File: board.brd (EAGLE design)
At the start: 50 x 50 mm, 28 parts

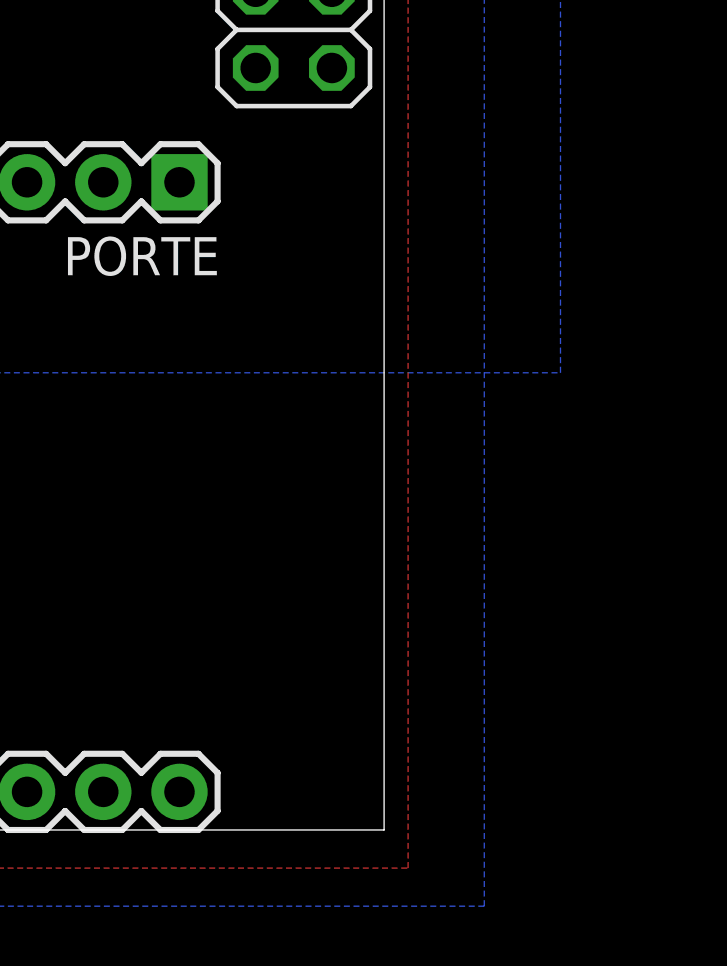
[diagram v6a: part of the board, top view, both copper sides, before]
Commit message: connecting rest of the ports
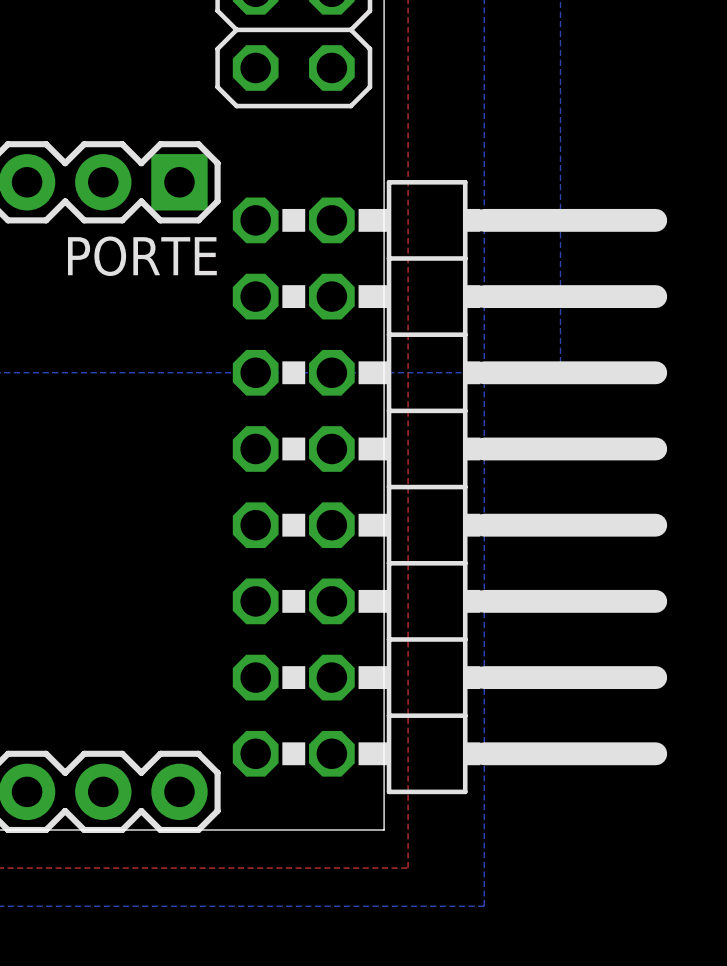
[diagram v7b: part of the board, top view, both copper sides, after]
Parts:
- added JP2: (no value), pinhead:2X08/90
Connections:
- removed net SCL: PORTE.2
- removed net SDA: PORTE.1
- new net PB1/VBAT_SENSE: JP2.3, PORTB.2
- new net PB2: JP2.5, PORTB.3
- new net PB3: JP2.7, PORTB.4
- new net PD0: JP2.9, PORTD.1
- new net PD1: JP2.11, PORTD.2
- new net PD5: JP2.15, PORTD.6
- new net PE1/SCL: JP2.4, PORTE.2
- new net PE1/SDA: JP2.2, PORTE.1
- new net PE2: JP2.6, PORTE.3
- new net PE3: JP2.8, PORTE.4
- net +3V3: now also JP2.12
- net GND: now also JP2.10, JP2.13
- net PB0/XMEGA_AREF: now also JP2.1
- net VBAT_SENSE: no longer PORTB.2
- net XMEGA_RX1: now also JP2.14
- net XMEGA_TX1: now also JP2.16
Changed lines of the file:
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@@
 <attribute name="VALUE" x="22.225" y="45.339" size="1.27" layer="27" rot="R270"/>
+</element>
+<element name="JP2" library="pinhead" package="2X08/90" value="" x="52.07" y="11.43" smashed="yes" rot="R270">
+<attribute name="VALUE" x="48.26" y="-0.635" size="1.27" layer="27"/>
 </element>
 </elements>
@@
 <contactref element="PGND_GND" pad="1"/>
 <contactref element="AGND_GND" pad="2"/>
+<contactref element="JP2" pad="10"/>
+<contactref element="JP2" pad="13"/>
 </signal>
 <signal name="PDI_DATA">
@@
 <wire x1="5.59" y1="26.465" x2="33.02" y2="1.27" width="0" layer="19" extent="1-1"/>
 </signal>
-<signal name="SDA">
+<signal name="PE1/SDA">
 <contactref element="PORTE" pad="1"/>
-</signal>
-<signal name="SCL">
+<contactref element="JP2" pad="2"/>
+<wire x1="43.18" y1="21.59" x2="48.26" y2="20.32" width="0" layer="19" extent="1-1"/>
+</signal>
+<signal name="PE1/SCL">
 <contactref element="PORTE" pad="2"/>
+<contactref element="JP2" pad="4"/>
+<wire x1="40.64" y1="21.59" x2="48.26" y2="17.78" width="0" layer="19" extent="1-1"/>
 </signal>
 <signal name="VXMEGA_USB">
@@
 <signal name="XMEGA_TX1">
 <contactref element="PORTC" pad="8"/>
+<contactref element="JP2" pad="16"/>
+<wire x1="22.86" y1="1.27" x2="48.26" y2="2.54" width="0" layer="19" extent="1-1"/>
 </signal>
 <signal name="XMEGA_RX1">
 <contactref element="PORTC" pad="7"/>
+<contactref element="JP2" pad="14"/>
+<wire x1="20.32" y1="1.27" x2="48.26" y2="5.08" width="0" layer="19" extent="1-1"/>
 </signal>
 <signal name="PGND" class="1">
@@
 <contactref element="R2" pad="2"/>
 <contactref element="C1" pad="1"/>
-<contactref element="PORTB" pad="2"/>
-<wire x1="10.16" y1="21.59" x2="9.765" y2="24.13" width="0" layer="19" extent="16-16"/>
-<wire x1="10.16" y1="18.73" x2="10.16" y2="21.59" width="0" layer="19" extent="16-16"/>
+<wire x1="10.16" y1="18.73" x2="9.765" y2="24.13" width="0" layer="19" extent="16-16"/>
 <wire x1="7.62" y1="18.73" x2="10.16" y2="18.73" width="0" layer="19" extent="16-16"/>
 </signal>
@@
 <contactref element="SJ2" pad="3"/>
 <contactref element="XBEE" pad="1"/>
+<contactref element="JP2" pad="12"/>
 <wire x1="1.59" y1="26.465" x2="22.86" y2="44.196" width="0" layer="19" extent="1-1"/>
+<wire x1="48.26" y1="7.62" x2="22.86" y2="44.196" width="0" layer="19" extent="1-1"/>
 </signal>
 <signal name="LED0R" class="1">
@@
 <contactref element="PORTB" pad="1"/>
 <contactref element="XBEE" pad="14"/>
-<wire x1="12.7" y1="21.59" x2="13.59" y2="48.465" width="0" layer="19" extent="1-1"/>
+<contactref element="JP2" pad="1"/>
+<wire x1="12.7" y1="21.59" x2="45.72" y2="20.32" width="0" layer="19" extent="1-1"/>
+<wire x1="13.59" y1="48.465" x2="12.7" y2="21.59" width="0" layer="19" extent="1-1"/>
 </signal>
 <signal name="XBEE_RESET">
@@
 <wire x1="9.59" y1="26.465" x2="35.56" y2="1.27" width="0" layer="19" extent="1-1"/>
 </signal>
+<signal name="PB1/VBAT_SENSE">
+<contactref element="PORTB" pad="2"/>
+<contactref element="JP2" pad="3"/>
+<wire x1="10.16" y1="21.59" x2="45.72" y2="17.78" width="0" layer="19" extent="1-1"/>
+</signal>
+<signal name="PB2">
+<contactref element="PORTB" pad="3"/>
+<contactref element="JP2" pad="5"/>
+<wire x1="7.62" y1="21.59" x2="45.72" y2="15.24" width="0" layer="19" extent="1-1"/>
+</signal>
+<signal name="PB3">
+<contactref element="PORTB" pad="4"/>
+<contactref element="JP2" pad="7"/>
+<wire x1="5.08" y1="21.59" x2="45.72" y2="12.7" width="0" layer="19" extent="1-1"/>
+</signal>
+<signal name="PE2">
+<contactref element="PORTE" pad="3"/>
+<contactref element="JP2" pad="6"/>
+<wire x1="38.1" y1="21.59" x2="48.26" y2="15.24" width="0" layer="19" extent="1-1"/>
+</signal>
+<signal name="PE3">
+<contactref element="PORTE" pad="4"/>
+<contactref element="JP2" pad="8"/>
+<wire x1="35.56" y1="21.59" x2="48.26" y2="12.7" width="0" layer="19" extent="1-1"/>
+</signal>
+<signal name="PD0">
+<contactref element="PORTD" pad="1"/>
+<contactref element="JP2" pad="9"/>
+<wire x1="25.4" y1="1.27" x2="45.72" y2="10.16" width="0" layer="19" extent="1-1"/>
+</signal>
+<signal name="PD1">
+<contactref element="PORTD" pad="2"/>
+<contactref element="JP2" pad="11"/>
+<wire x1="27.94" y1="1.27" x2="45.72" y2="7.62" width="0" layer="19" extent="1-1"/>
+</signal>
+<signal name="PD5">
+<contactref element="PORTD" pad="6"/>
+<contactref element="JP2" pad="15"/>
+<wire x1="38.1" y1="1.27" x2="45.72" y2="2.54" width="0" layer="19" extent="1-1"/>
+</signal>
 </signals>

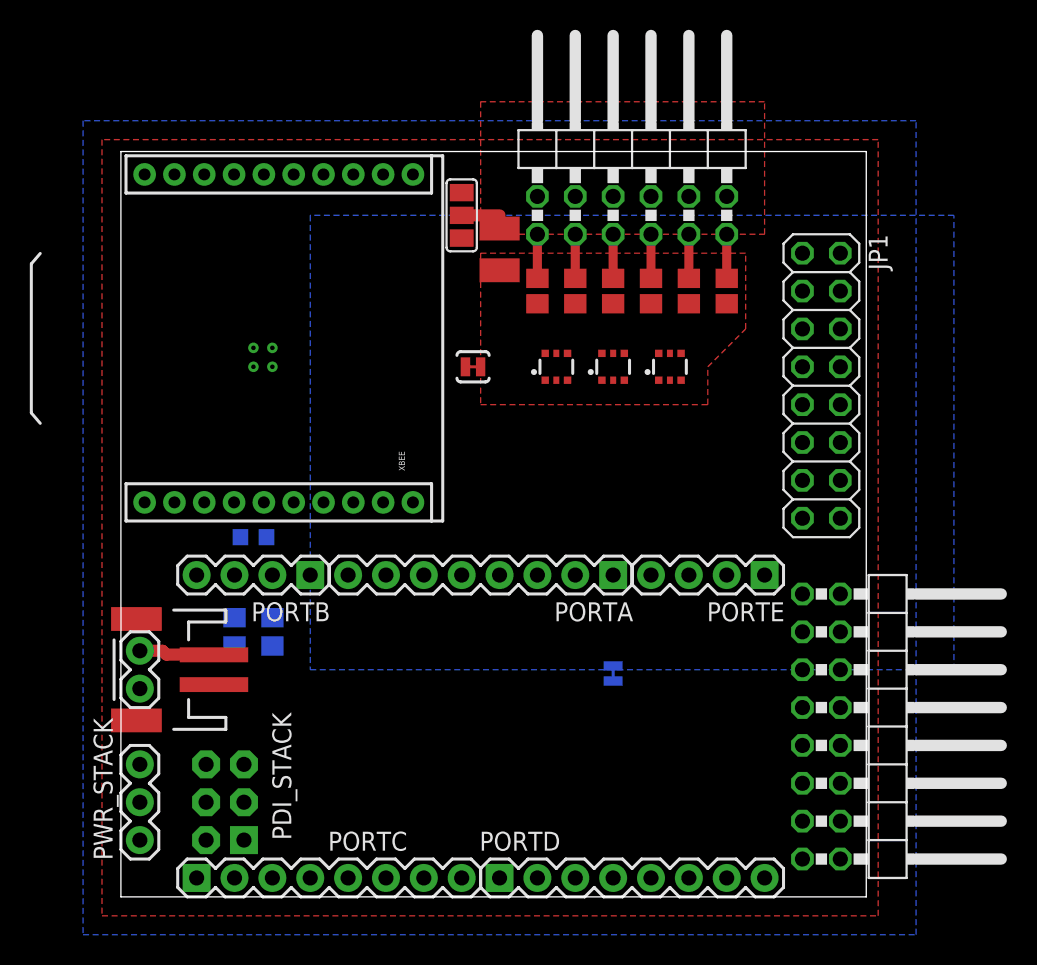
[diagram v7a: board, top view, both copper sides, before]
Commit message: adjust the AGND polygon
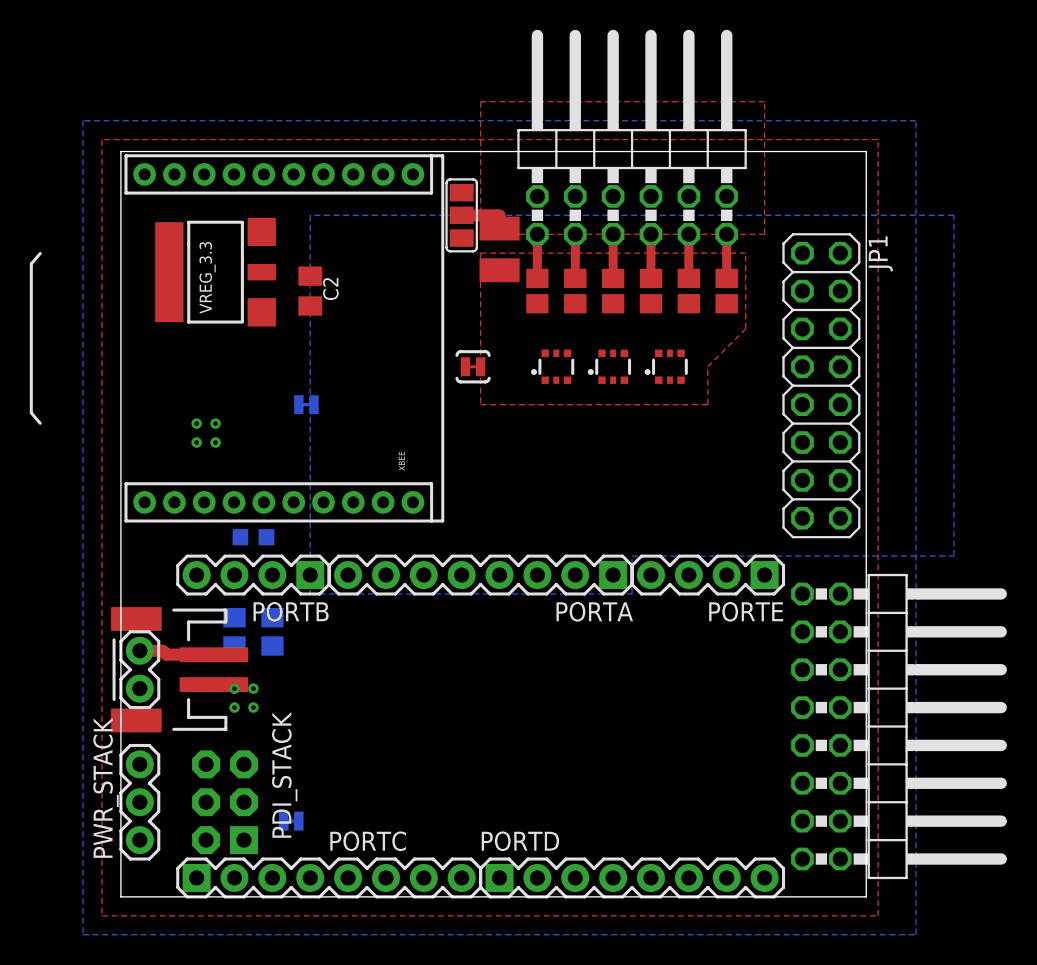
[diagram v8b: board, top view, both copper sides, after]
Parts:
- added +3.3V_VXMEGA: SOLDERJUMPERTRACE, SparkFun-Passives:SJ_2S-TRACE
- added C2: (no value), rcl:C0805K
- added VREG_3.3: (no value), microbuilder:SOT223-W
- moved AGND_GND 27.4 mm to (12.4, 33.0), turned to 0 degrees
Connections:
- net +3V3: now also +3.3V_VXMEGA.1, C2.1, VREG_3.3.2
- net GND: now also C2.2, VREG_3.3.1
- net VBAT: now also VREG_3.3.3
- net VXMEGA: now also +3.3V_VXMEGA.2
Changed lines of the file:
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@@
 <attribute name="VALUE" x="43.815" y="46.99" size="1.27" layer="27" rot="R90"/>
 </element>
-<element name="AGND_GND" library="SparkFun-Passives" package="SJ_2S-TRACE" value="SOLDERJUMPERTRACE" x="33.02" y="14.986" smashed="yes" rot="MR270"/>
+<element name="AGND_GND" library="SparkFun-Passives" package="SJ_2S-TRACE" value="SOLDERJUMPERTRACE" x="12.446" y="33.02" smashed="yes" rot="MR0"/>
 <element name="C3" library="rcl" package="C1210" value="" x="25.4" y="43.434" smashed="yes" rot="R270">
 <attribute name="VALUE" x="22.225" y="45.339" size="1.27" layer="27" rot="R270"/>
@@
 <attribute name="VALUE" x="48.26" y="-0.635" size="1.27" layer="27"/>
 </element>
+<element name="VREG_3.3" library="microbuilder" package="SOT223-W" value="" x="6.35" y="41.91" rot="R90"/>
+<element name="+3.3V_VXMEGA" library="SparkFun-Passives" package="SJ_2S-TRACE" value="SOLDERJUMPERTRACE" x="11.43" y="5.08" smashed="yes" rot="MR0"/>
+<element name="C2" library="rcl" package="C0805K" value="" x="12.7" y="40.64" rot="R270"/>
 </elements>
 <signals>
@@
 <contactref element="R2" pad="1"/>
 <contactref element="C1" pad="2"/>
-<via x="8.89" y="35.56" extent="1-16" drill="0.3048"/>
-<via x="10.16" y="35.56" extent="1-16" drill="0.3048"/>
-<via x="10.16" y="36.83" extent="1-16" drill="0.3048"/>
-<via x="8.89" y="36.83" extent="1-16" drill="0.3048"/>
+<via x="5.08" y="30.48" extent="1-16" drill="0.3048"/>
+<via x="6.35" y="30.48" extent="1-16" drill="0.3048"/>
+<via x="6.35" y="31.75" extent="1-16" drill="0.3048"/>
+<via x="5.08" y="31.75" extent="1-16" drill="0.3048"/>
 <contactref element="PGND_GND" pad="1"/>
 <contactref element="AGND_GND" pad="2"/>
 <contactref element="JP2" pad="10"/>
 <contactref element="JP2" pad="13"/>
+<contactref element="VREG_3.3" pad="1"/>
+<contactref element="C2" pad="2"/>
+<via x="7.62" y="12.7" extent="1-16" drill="0.3048"/>
+<via x="8.89" y="12.7" extent="1-16" drill="0.3048"/>
+<via x="8.89" y="13.97" extent="1-16" drill="0.3048"/>
+<via x="7.62" y="13.97" extent="1-16" drill="0.3048"/>
 </signal>
 <signal name="PDI_DATA">
@@
 <contactref element="PDI_STACK" pad="2"/>
 <contactref element="PWR_STACK" pad="3"/>
+<contactref element="+3.3V_VXMEGA" pad="2"/>
+<wire x1="5.715" y1="3.81" x2="10.922" y2="5.08" width="0" layer="19" extent="16-16"/>
 <wire x1="1.27" y1="8.89" x2="5.715" y2="3.81" width="0" layer="19" extent="1-1"/>
 </signal>
@@
 <wire x1="3.048" y1="16.256" x2="6.224" y2="16.256" width="0.8128" layer="1"/>
 <wire x1="6.224" y1="16.256" x2="6.24" y2="16.24" width="0.8128" layer="1"/>
-<wire x1="7.62" y1="16.83" x2="22.86" y2="47.244" width="0" layer="19" extent="1-16"/>
+<contactref element="VREG_3.3" pad="3"/>
+<wire x1="9.45" y1="44.61" x2="22.86" y2="47.244" width="0" layer="19" extent="1-1"/>
+<wire x1="7.62" y1="16.83" x2="9.45" y2="44.61" width="0" layer="19" extent="1-16"/>
 <wire x1="6.24" y1="16.51" x2="7.62" y2="16.83" width="0" layer="19" extent="1-16"/>
 </signal>
@@
 <vertex x="55.88" y="45.72"/>
 <vertex x="12.7" y="45.72"/>
-<vertex x="12.7" y="15.24"/>
-<vertex x="55.88" y="15.24"/>
+<vertex x="12.7" y="20.32"/>
+<vertex x="34.29" y="20.32"/>
+<vertex x="34.29" y="22.86"/>
+<vertex x="55.88" y="22.86"/>
 </polygon>
 <contactref element="AGND_GND" pad="1"/>
@@
 <wire x1="37.58" y1="34.66" x2="40.64" y2="39.79" width="0" layer="19" extent="1-1"/>
 </signal>
-<signal name="+3V3">
+<signal name="+3V3" class="1">
 <contactref element="SJ2" pad="3"/>
 <contactref element="XBEE" pad="1"/>
 <contactref element="JP2" pad="12"/>
-<wire x1="1.59" y1="26.465" x2="22.86" y2="44.196" width="0" layer="19" extent="1-1"/>
-<wire x1="48.26" y1="7.62" x2="22.86" y2="44.196" width="0" layer="19" extent="1-1"/>
+<contactref element="VREG_3.3" pad="2"/>
+<contactref element="+3.3V_VXMEGA" pad="1"/>
+<contactref element="C2" pad="1"/>
+<wire x1="12.7" y1="41.64" x2="22.86" y2="44.196" width="0" layer="19" extent="1-1"/>
+<wire x1="9.45" y1="41.91" x2="12.7" y2="41.64" width="0" layer="19" extent="1-1"/>
+<wire x1="1.59" y1="26.465" x2="9.45" y2="41.91" width="0" layer="19" extent="1-1"/>
+<wire x1="11.938" y1="5.08" x2="1.59" y2="26.465" width="0" layer="19" extent="16-16"/>
+<wire x1="48.26" y1="7.62" x2="11.938" y2="5.08" width="0" layer="19" extent="16-16"/>
 </signal>
 <signal name="LED0R" class="1">
